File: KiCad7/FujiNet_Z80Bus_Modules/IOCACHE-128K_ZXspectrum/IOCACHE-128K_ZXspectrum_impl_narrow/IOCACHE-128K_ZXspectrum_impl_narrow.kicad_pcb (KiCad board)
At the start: 2 copper layers, 45 x 95 mm, 6 parts, among them IC1 74HC590N, IC2 74HC590N, J1 Conn_01x14_Socket, J2 Conn_01x24_Socket

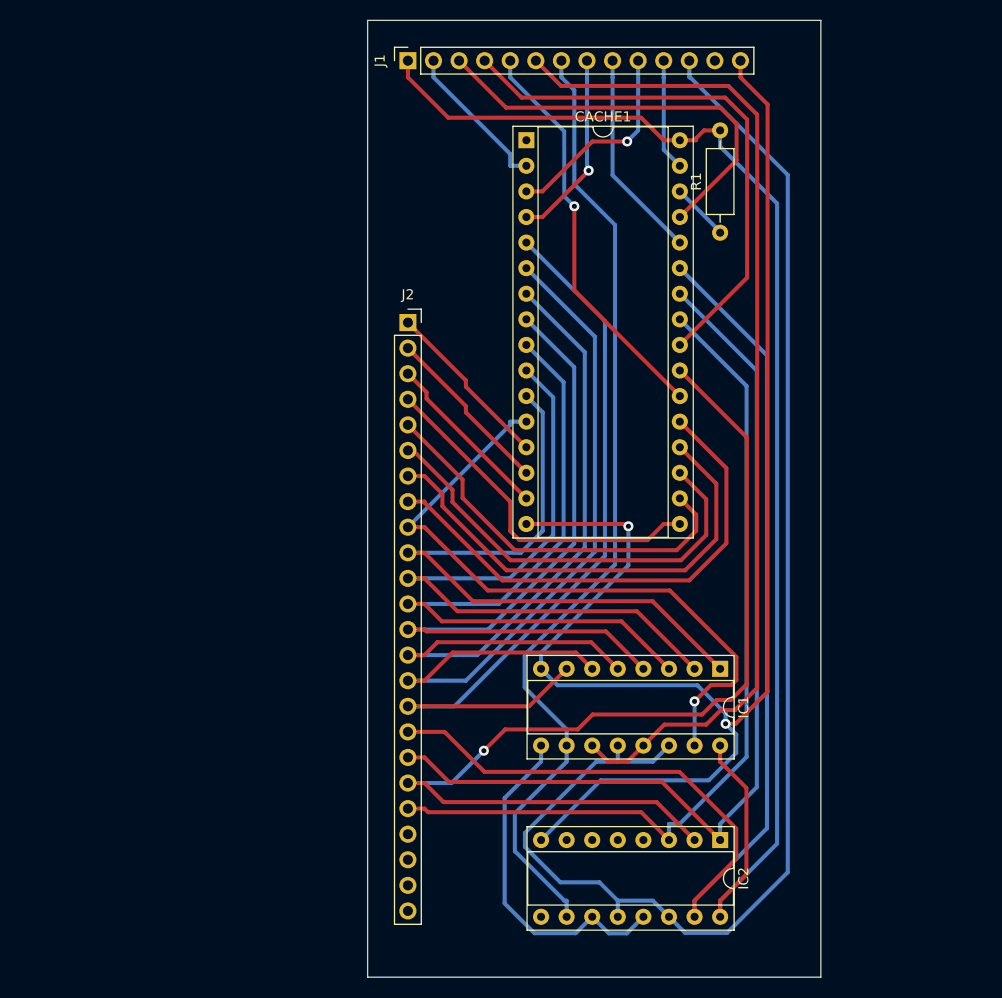
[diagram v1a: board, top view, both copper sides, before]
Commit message: KiCad Corrected the orientation of the impl PCBs
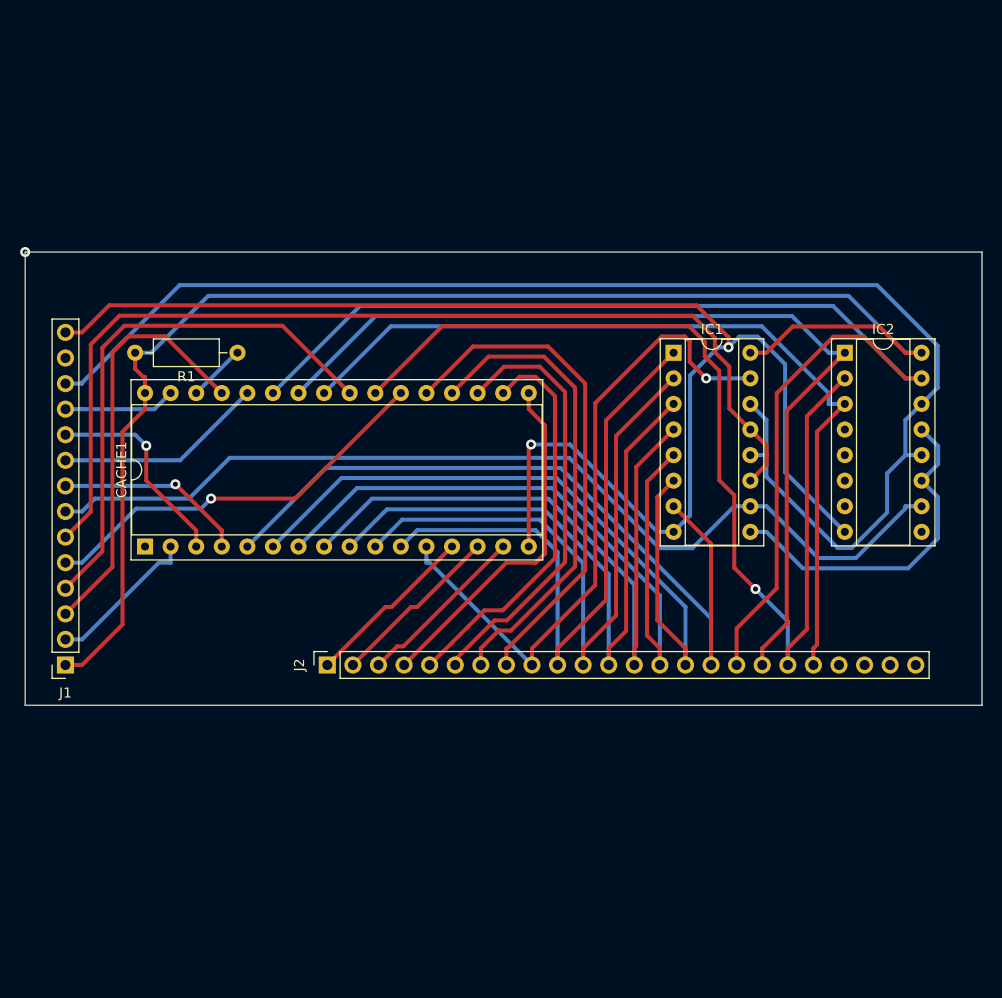
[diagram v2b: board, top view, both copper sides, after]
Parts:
- moved J1 69.0 mm to (84.0, 129.0), turned to 180 degrees
- moved CACHE1 55.3 mm to (91.9, 117.2), turned to 90 degrees
- moved IC2 49.9 mm to (161.4, 98.0), turned to 0 degrees
- moved R1 49.4 mm to (101.1, 98.0), turned to 180 degrees
- moved J2 34.9 mm to (110.0, 129.0), turned to 90 degrees
- moved IC1 31.7 mm to (144.4, 98.0), turned to 0 degrees
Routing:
- net (no net): vias 0 -> 1
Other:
- board size 45 x 95 mm -> 95 x 45 mm

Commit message: KICAD IOCACHE fixed
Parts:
- removed J1: Conn_01x14_Socket, Connector_PinSocket_2.54mm:PinSocket_1x14_P2.54mm_Vertical
- removed J2: Conn_01x24_Socket, Connector_PinSocket_2.54mm:PinSocket_1x24_P2.54mm_Vertical
- added CACHE2: Conn_01x24_Socket, Connector_PinSocket_2.54mm:PinSocket_1x24_P2.54mm_Vertical, F.Cu at (110.0, 129.0)
- added CACHE3: Conn_01x14_Socket, Connector_PinSocket_2.54mm:PinSocket_1x14_P2.54mm_Vertical, F.Cu at (84.0, 96.0)
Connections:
- CACHE1 pad 28: /IOCACHE-128K_ZXspectrum/CACHE_SEL_1 -> /IOCACHE-128K_ZXspectrum/LOCAL_A13
- CACHE1 pad 3: /IOCACHE-128K_ZXspectrum/CACHE_SEL_2 -> /IOCACHE-128K_ZXspectrum/LOCAL_A14
- CACHE1 pad 31: /IOCACHE-128K_ZXspectrum/CACHE_SEL_3 -> /IOCACHE-128K_ZXspectrum/LOCAL_A15
- CACHE1 pad 4: /IOCACHE-128K_ZXspectrum/CACHE_SEL_0 -> /IOCACHE-128K_ZXspectrum/LOCAL_A12
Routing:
- net /IOCACHE-128K_ZXspectrum/LOCAL_A13: track 0.00 -> 147.8 mm
- net /IOCACHE-128K_ZXspectrum/LOCAL_A15: track 0.00 -> 111.7 mm, vias 0 -> 1
- net /IOCACHE-128K_ZXspectrum/LOCAL_A14: track 0.00 -> 90.2 mm, vias 0 -> 1
- net /IOCACHE-128K_ZXspectrum/LOCAL_A12: track 0.00 -> 84.8 mm, vias 0 -> 1
- net GND: track 144.7 -> 96.7 mm, vias 2 -> 0
- net /IOCACHE-128K_ZXspectrum/LOCAL_A11: track 85.5 -> 131.1 mm
- net /IOCACHE-128K_ZXspectrum/CACHE_CONTROL.WE: track 41.7 -> 17.3 mm
- net /IOCACHE-128K_ZXspectrum/CACHE_CONTROL.OE: track 53.6 -> 29.7 mm
- net +5V: track 137.7 -> 115.8 mm
- net /IOCACHE-128K_ZXspectrum/CACHE_SEL_1: track 20.8 -> 0.00 mm
- net /IOCACHE-128K_ZXspectrum/CACHE_DATASTATUS: track 139.3 -> 118.6 mm
- net /IOCACHE-128K_ZXspectrum/CACHE_SEL_2: track 20.5 -> 0.00 mm, vias 1 -> 0
- net /IOCACHE-128K_ZXspectrum/CACHE_SEL_0: track 19.1 -> 0.00 mm, vias 1 -> 0
- net /IOCACHE-128K_ZXspectrum/Z80_HARDLOCK: track 97.0 -> 113.9 mm, vias 0 -> 1
- net /IOCACHE-128K_ZXspectrum/LOCAL_A7: track 77.4 -> 63.8 mm, vias 0 -> 1
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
